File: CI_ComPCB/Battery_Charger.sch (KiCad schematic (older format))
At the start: 5 parts, among them Q201 Transistor_FET_IRF9540N

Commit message: V1.1 in progress
Completed Bom and schematic
still need to add routs and PCB layout
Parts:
- Q201: JLCPCB (none) -> C2575
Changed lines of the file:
@@
 F 2 "Package_TO_SOT_THT:TO-220-3_Vertical" H 5100 3265 50  0001 L CIN
 F 3 "" H 4900 3340 50  0001 L CNN
+F 4 "C2575" V 4900 3340 50  0001 C CNN "JLCPCB"
 	1    4900 3340
 	0    -1   -1   0
+$EndComp
+$Comp
+L Device:R R?
+U 1 1 61A36CED
+P 4550 3540
+AR Path="/61A36CED" Ref="R?"  Part="1"
+AR Path="/61A30F2E/61A36CED" Ref="R201"  Part="1"
+F 0 "R201" H 4620 3586 50  0000 L CNN
+F 1 "330" H 4620 3495 50  0000 L CNN
+F 2 "Resistor_SMD:R_0805_2012Metric" V 4480 3540 50  0001 C CNN
+F 3 "~" H 4550 3540 50  0001 C CNN
+	1    4550 3540
+	0    1    1    0
+$EndComp
+$Comp
+L power:GND #PWR?
+U 1 1 61A36CE7
+P 4400 3540
+AR Path="/61A36CE7" Ref="#PWR?"  Part="1"
+AR Path="/61A30F2E/61A36CE7" Ref="#PWR0201"  Part="1"
+F 0 "#PWR0201" H 4400 3290 50  0001 C CNN
+F 1 "GND" H 4405 3367 50  0000 C CNN
+F 2 "" H 4400 3540 50  0001 C CNN
+F 3 "" H 4400 3540 50  0001 C CNN
+	1    4400 3540
+	1    0    0    -1
 $EndComp
 $Comp
@@
 	0    1    1    0
 $EndComp
-$Comp
-L power:GND #PWR?
-U 1 1 61A36CE7
-P 4400 3540
-AR Path="/61A36CE7" Ref="#PWR?"  Part="1"
-AR Path="/61A30F2E/61A36CE7" Ref="#PWR0201"  Part="1"
-F 0 "#PWR0201" H 4400 3290 50  0001 C CNN
-F 1 "GND" H 4405 3367 50  0000 C CNN
-F 2 "" H 4400 3540 50  0001 C CNN
-F 3 "" H 4400 3540 50  0001 C CNN
-	1    4400 3540
-	1    0    0    -1
-$EndComp
-$Comp
-L Device:R R?
-U 1 1 61A36CED
-P 4550 3540
-AR Path="/61A36CED" Ref="R?"  Part="1"
-AR Path="/61A30F2E/61A36CED" Ref="R201"  Part="1"
-F 0 "R201" H 4620 3586 50  0000 L CNN
-F 1 "330" H 4620 3495 50  0000 L CNN
-F 2 "Resistor_SMD:R_0805_2012Metric" V 4480 3540 50  0001 C CNN
-F 3 "~" H 4550 3540 50  0001 C CNN
-	1    4550 3540
-	0    1    1    0
-$EndComp

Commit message: V1.1 Rough
Almost complete
needs silk screen annotations then will be ready to have printed
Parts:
- D201: symbol dk_LED-Indication-Discrete:LTST-C190GKT -> CI_ComPCB-rescue:LTST-C190GKT-dk_LED-Indication-Discrete
- HW-201: symbol CI_ComPCB-rescue:Charger-New_Library-RackComm-rescue-RackComm-rescue -> CI_ComPCB-rescue:Charger-New_Library-RackComm-rescue-RackComm-rescue-CI_ComPCB-rescue
- Holder201: symbol CI_ComPCB-rescue:Battery-New_Library-RackComm-rescue -> CI_ComPCB-rescue:Battery-New_Library-RackComm-rescue-CI_ComPCB-rescue
- Q201: symbol CI_ComPCB-cache:Transistor_FET_IRF9540N -> CI_ComPCB-rescue:Transistor_FET_IRF9540N-CI_ComPCB-cache
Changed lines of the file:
@@
 $EndDescr
 $Comp
-L CI_ComPCB-rescue:Charger-New_Library-RackComm-rescue-RackComm-rescue HW-?
+L CI_ComPCB-rescue:Charger-New_Library-RackComm-rescue-RackComm-rescue-CI_ComPCB-rescue HW-?
 U 1 1 61A36CB0
 P 6450 2780
@@
 $EndComp
 $Comp
-L CI_ComPCB-rescue:Battery-New_Library-RackComm-rescue Holder?
+L CI_ComPCB-rescue:Battery-New_Library-RackComm-rescue-CI_ComPCB-rescue Holder?
 U 1 1 61A36CB6
 P 6200 3580
@@
 Battery_Power
 $Comp
-L CI_ComPCB-cache:Transistor_FET_IRF9540N Q?
+L CI_ComPCB-rescue:Transistor_FET_IRF9540N-CI_ComPCB-cache Q?
 U 1 1 61A36CD2
 P 4900 3340
@@
 $EndComp
 $Comp
-L dk_LED-Indication-Discrete:LTST-C190GKT D?
+L CI_ComPCB-rescue:LTST-C190GKT-dk_LED-Indication-Discrete D?
 U 1 1 61A36CE1
 P 4700 3440

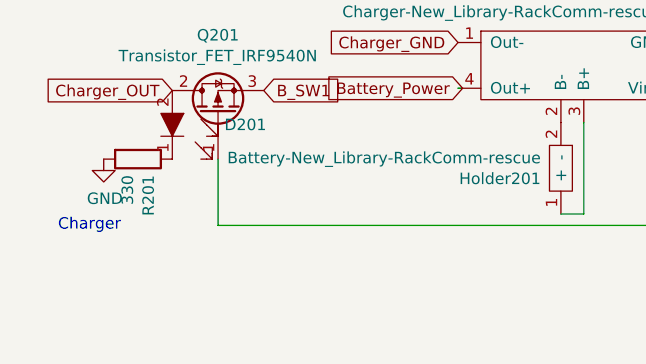
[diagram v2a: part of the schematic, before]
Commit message: V1.1 board
Board is ready to print
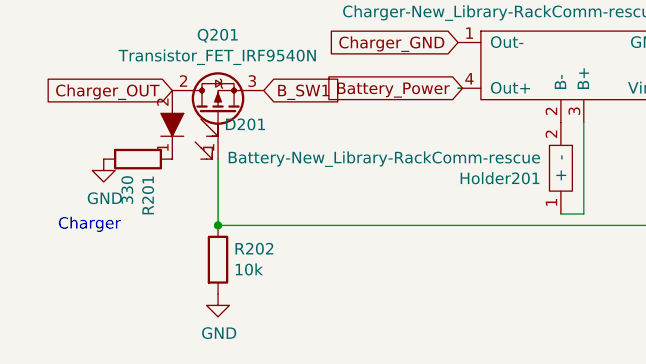
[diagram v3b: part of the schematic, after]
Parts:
- added R202: 10k, Resistor_SMD:R_0805_2012Metric, symbol Device:R
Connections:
- net Charger_IN: now also R202.1
- net GND: now also R202.2
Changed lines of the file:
@@
 	0    1    1    0
 $EndComp
+$Comp
+L Device:R R202
+U 1 1 612D1327
+P 4900 3980
+F 0 "R202" H 4970 4026 50  0000 L CNN
+F 1 "10k" H 4970 3935 50  0000 L CNN
+F 2 "Resistor_SMD:R_0805_2012Metric" V 4830 3980 50  0001 C CNN
+F 3 "~" H 4900 3980 50  0001 C CNN
+	1    4900 3980
+	1    0    0    -1
+$EndComp
+Connection ~ 4900 3830
+$Comp
+L power:GND #PWR0105
+U 1 1 612D1AE2
+P 4900 4130
+F 0 "#PWR0105" H 4900 3880 50  0001 C CNN
+F 1 "GND" H 4905 3957 50  0000 C CNN
+F 2 "" H 4900 4130 50  0001 C CNN
+F 3 "" H 4900 4130 50  0001 C CNN
+	1    4900 4130
+	1    0    0    -1
+$EndComp
 $EndSCHEMATC

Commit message: stuff
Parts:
- removed HW-201: Charger-New_Library-RackComm-rescue-RackComm-resc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, CI_ComPCB:Charger, symbol CI_ComPCB-rescue:Charger-New_Library-RackComm-rescue-RackComm-rescue-CI_ComPCB-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
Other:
- note added: "https://www.amazon.com/DGZZI-Charger-Lithium-Battery-Protection/dp/B07RKL438C/ref=sr_1_4?crid=1OYPBW1QQ1WYA&keywords=10A+BMS+Charger+Protection+Board+for+Pack+of+3+18650+Li-ion+lithium+Battery+Cell&qid=1636155931&sprefix=10a+bms+charger+protection+board+for+pack+of+3+18650+li-ion+lithium+battery+cell%2Caps%2C91&sr=8-4"
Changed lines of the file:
@@
 $Descr A4 11693 8268
 encoding utf-8
-Sheet 2 6
+Sheet 2 5
 Title ""
 Date ""
@@
 Comment4 ""
 $EndDescr
-$Comp
-L CI_ComPCB-rescue:Charger-New_Library-RackComm-rescue-RackComm-rescue-CI_ComPCB-rescue HW-?
-U 1 1 61A36CB0
-P 6450 2780
-AR Path="/61A36CB0" Ref="HW-?"  Part="1"
-AR Path="/61A30F2E/61A36CB0" Ref="HW-201"  Part="1"
-F 0 "HW-201" H 6475 2755 50  0000 C CNN
-F 1 "Charger-New_Library-RackComm-rescue-RackComm-rescue" H 6475 2664 50  0000 C CNN
-F 2 "CI_ComPCB:Charger" H 6450 2780 50  0001 C CNN
-F 3 "" H 6450 2780 50  0001 C CNN
-	1    6450 2780
-	1    0    0    -1
-$EndComp
 $Comp
 L CI_ComPCB-rescue:Battery-New_Library-RackComm-rescue-CI_ComPCB-rescue Holder?
@@
 	4900 3540 4900 3830
 Wire Wire Line
-	4900 3830 7000 3830
+	5432 4700 7532 4700
 Wire Wire Line
-	7000 3830 7000 3230
+	7532 4700 7532 4100
 $Comp
 L power:GND #PWR?
 U 1 1 61A36CC1
-P 7000 3030
+P 7532 3900
 AR Path="/61A36CC1" Ref="#PWR?"  Part="1"
 AR Path="/61A30F2E/61A36CC1" Ref="#PWR0202"  Part="1"
-F 0 "#PWR0202" H 7000 2780 50  0001 C CNN
-F 1 "GND" H 7005 2857 50  0000 C CNN
-F 2 "" H 7000 3030 50  0001 C CNN
-F 3 "" H 7000 3030 50  0001 C CNN
-	1    7000 3030
+F 0 "#PWR0202" H 7532 3650 50  0001 C CNN
+F 1 "GND" H 7537 3727 50  0000 C CNN
+F 2 "" H 7532 3900 50  0001 C CNN
+F 3 "" H 7532 3900 50  0001 C CNN
+	1    7532 3900
 	0    -1   -1   0
 $EndComp
@@
 Text Notes 4200 3860 0    50   ~ 0
 Charger
-Text GLabel 7000 3230 2    50   Input ~ 0
+Text GLabel 7532 4100 2    50   Input ~ 0
 Charger_IN
 Text GLabel 5970 3230 0    50   Input ~ 0
@@
 	1    0    0    -1
 $EndComp
-Connection ~ 4900 3830
 $Comp
 L power:GND #PWR0105
@@
 	1    0    0    -1
 $EndComp
+Text Notes 7216 6154 0    50   ~ 0
+https://www.amazon.com/DGZZI-Charger-Lithium-Battery-Protection/dp/B07RKL438C/ref=sr_1_4?crid=1OYPBW1QQ1WYA&keywords=10A+BMS+Charger+Protection+Board+for+Pack+of+3+18650+Li-ion+lithium+Battery+Cell&qid=1636155931&sprefix=10a+bms+charger+protection+board+for+pack+of+3+18650+li-ion+lithium+battery+cell%2Caps%2C91&sr=8-4
 $EndSCHEMATC

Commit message: a
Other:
- note added: "https://www.amazon.com/Li-ion-Lithium-Battery-Charger-Protection/dp/B085WBC3VD/ref=pd_sbs_4/142-9960783-6429120?pd_rd_w=BQDWq&pf_rd_p=8b76d7a7-ab83-4ddc-a92d-e3e33bfdbf03&pf_rd_r=1G7PKXSWC24V1T78R90V&pd_rd_r=f6b41e4c-7f01-498a-b560-66b727321cd4&pd_rd_wg=bSg1c&pd_rd_i=B085WBC3VD&psc=1"
- note removed: "https://www.amazon.com/DGZZI-Charger-Lithium-Battery-Protection/dp/B07RKL438C/ref=sr_1_4?crid=1OYPBW1QQ1WYA&keywords=10A+BMS+Charger+Protection+Board+for+Pack+of+3+18650+Li-ion+lithium+Battery+Cell&qid=1636155931&sprefix=10a+bms+charger+protection+board+for+pack+of+3+18650+li-ion+lithium+battery+cell%2Caps%2C91&sr=8-4"
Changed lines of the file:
@@
 $EndComp
 Text Notes 7216 6154 0    50   ~ 0
-https://www.amazon.com/DGZZI-Charger-Lithium-Battery-Protection/dp/B07RKL438C/ref=sr_1_4?crid=1OYPBW1QQ1WYA&keywords=10A+BMS+Charger+Protection+Board+for+Pack+of+3+18650+Li-ion+lithium+Battery+Cell&qid=1636155931&sprefix=10a+bms+charger+protection+board+for+pack+of+3+18650+li-ion+lithium+battery+cell%2Caps%2C91&sr=8-4
+https://www.amazon.com/Li-ion-Lithium-Battery-Charger-Protection/dp/B085WBC3VD/ref=pd_sbs_4/142-9960783-6429120?pd_rd_w=BQDWq&pf_rd_p=8b76d7a7-ab83-4ddc-a92d-e3e33bfdbf03&pf_rd_r=1G7PKXSWC24V1T78R90V&pd_rd_r=f6b41e4c-7f01-498a-b560-66b727321cd4&pd_rd_wg=bSg1c&pd_rd_i=B085WBC3VD&psc=1
 $EndSCHEMATC

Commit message: Sensor_SplitterPrint
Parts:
- D201: symbol CI_ComPCB-rescue:LTST-C190GKT-dk_LED-Indication-Discrete -> CI_ComPCB-rescue:LTST-C190GKT-dk_LED-Indication-Discrete-CI_ComPCB-rescue
- Holder201: symbol CI_ComPCB-rescue:Battery-New_Library-RackComm-rescue-CI_ComPCB-rescue -> CI_ComPCB-rescue:Battery-New_Library-RackComm-rescue-CI_ComPCB-rescue-CI_ComPCB-rescue
- Q201: symbol CI_ComPCB-rescue:Transistor_FET_IRF9540N-CI_ComPCB-cache -> CI_ComPCB-rescue:Transistor_FET_IRF9540N-CI_ComPCB-cache-CI_ComPCB-rescue
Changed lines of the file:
@@
 $EndDescr
 $Comp
-L CI_ComPCB-rescue:Battery-New_Library-RackComm-rescue-CI_ComPCB-rescue Holder?
+L CI_ComPCB-rescue:Battery-New_Library-RackComm-rescue-CI_ComPCB-rescue-CI_ComPCB-rescue Holder?
 U 1 1 61A36CB6
 P 6200 3580
@@
 Battery_Power
 $Comp
-L CI_ComPCB-rescue:Transistor_FET_IRF9540N-CI_ComPCB-cache Q?
+L CI_ComPCB-rescue:Transistor_FET_IRF9540N-CI_ComPCB-cache-CI_ComPCB-rescue Q?
 U 1 1 61A36CD2
 P 4900 3340
@@
 $EndComp
 $Comp
-L CI_ComPCB-rescue:LTST-C190GKT-dk_LED-Indication-Discrete D?
+L CI_ComPCB-rescue:LTST-C190GKT-dk_LED-Indication-Discrete-CI_ComPCB-rescue D?
 U 1 1 61A36CE1
 P 4700 3440
